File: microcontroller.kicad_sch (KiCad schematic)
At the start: 41 parts, among them U2 W25Q64JVSSIQ, U3 RP2350A, X1 ABM8-272-T3

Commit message: Rev3 fixes
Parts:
- removed R10, R11: 33k, Resistor_SMD:R_0603_1608Metric, symbol Device:R
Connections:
- net CAN_INT: now reaches U3.12 (GPIO8)
- net CAN_RESET: now reaches U3.13 (GPIO9)
- net CAN_STBY: now reaches U3.19 (GPIO15)
- net TX0RTS: now reaches U3.27 (GPIO16)
- net RX0BF: now reaches U3.28 (GPIO17)
- net RX1BF: now reaches U3.29 (GPIO18)
- net SCK: now reaches U3.4 (GPIO2)
- net MOSI: now reaches U3.5 (GPIO3)
- net MISO: now reaches U3.7 (GPIO4)
- net CS: now reaches U3.8 (GPIO5)
- net BUS1.SCL: no longer names the net of U3.35 (GPIO23)
- net BUS1.SDA: no longer names the net of U3.34 (GPIO22)
- no-connect marks 12 -> 6
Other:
- note removed: "I2C0 bus for external comms"
- moved on the sheet: R5, R6, R7, R8, R9

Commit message: Adding in JST XH
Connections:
- net CAN_INT: now also U3.8 (GPIO5); no longer U3.12 (GPIO8)
- net CAN_STBY: no longer U3.19 (GPIO15)
- net CS: now also U3.12 (GPIO8); no longer U3.8 (GPIO5)
- net RX0BF: no longer U3.28 (GPIO17)
- net RX1BF: no longer U3.29 (GPIO18)
- net TX0RTS: no longer U3.27 (GPIO16)
- no-connect marks 6 -> 14

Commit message: Adding JST XH and moving test points
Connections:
- no-connect marks 14 -> 13
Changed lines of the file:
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@@
 		(at 166.37 163.83)
-	)
-	(no_connect
-		(at 59.69 204.47)
 	)
 	(bus_entry

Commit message: Finalizing BOM
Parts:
- R8, R9: value 33k -> 10k; Mfr P/N RC0603FR-0733KL -> RT0603BRD0710KL; Supplier_1 P/N 311-33.0KHRTR-ND -> YAG1236TR-ND; Supplier_1 Unit Price 0.10000 -> 0.11; Supplier_2 P/N C126359 -> C95204; Supplier_2 Unit Price 0.0015 -> 0.0216
- renumbered R12 to R10, R13 to R11, R14 to R12, R15 to R13, R16 to R14, R17 to R15, R18 to R16, R19 to R17, R20 to R18, R21 to R19, U2 to U1, U3 to U2
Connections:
- net +3V3: now also R9.2; no longer R9.1
- net BUS0.SCL: now also R9.1; no longer R9.2

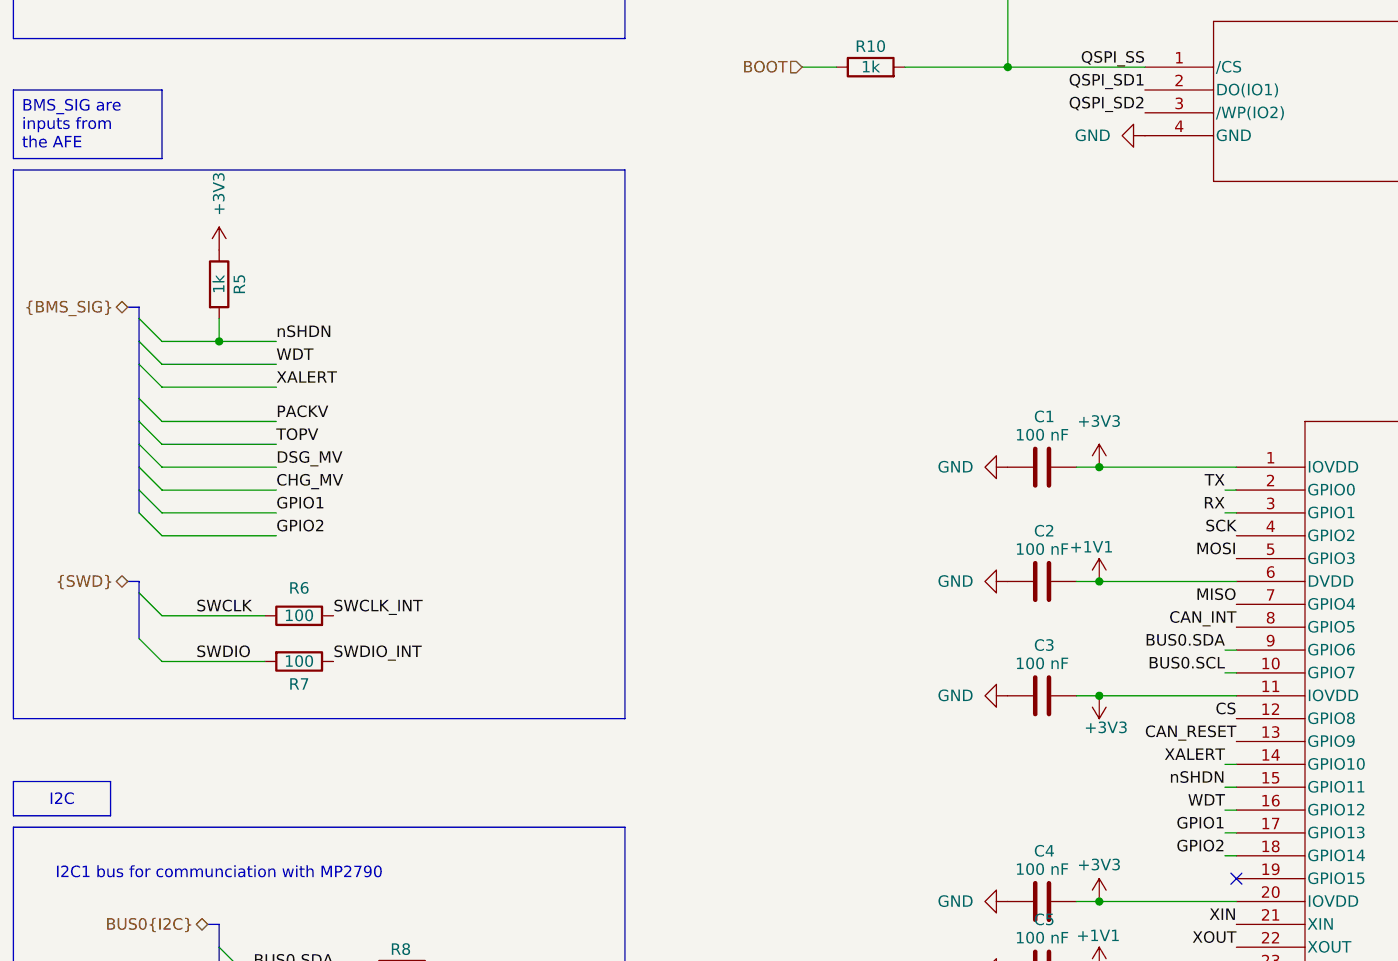
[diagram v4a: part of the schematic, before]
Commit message: rev3: nSHDN wake divider (1M/200k, 10k series to GPIO11), R_REG 100R 2512, 51R balance resistors, NTC ground resistors DNP, SMBJ28CA on TOP, BOM updates
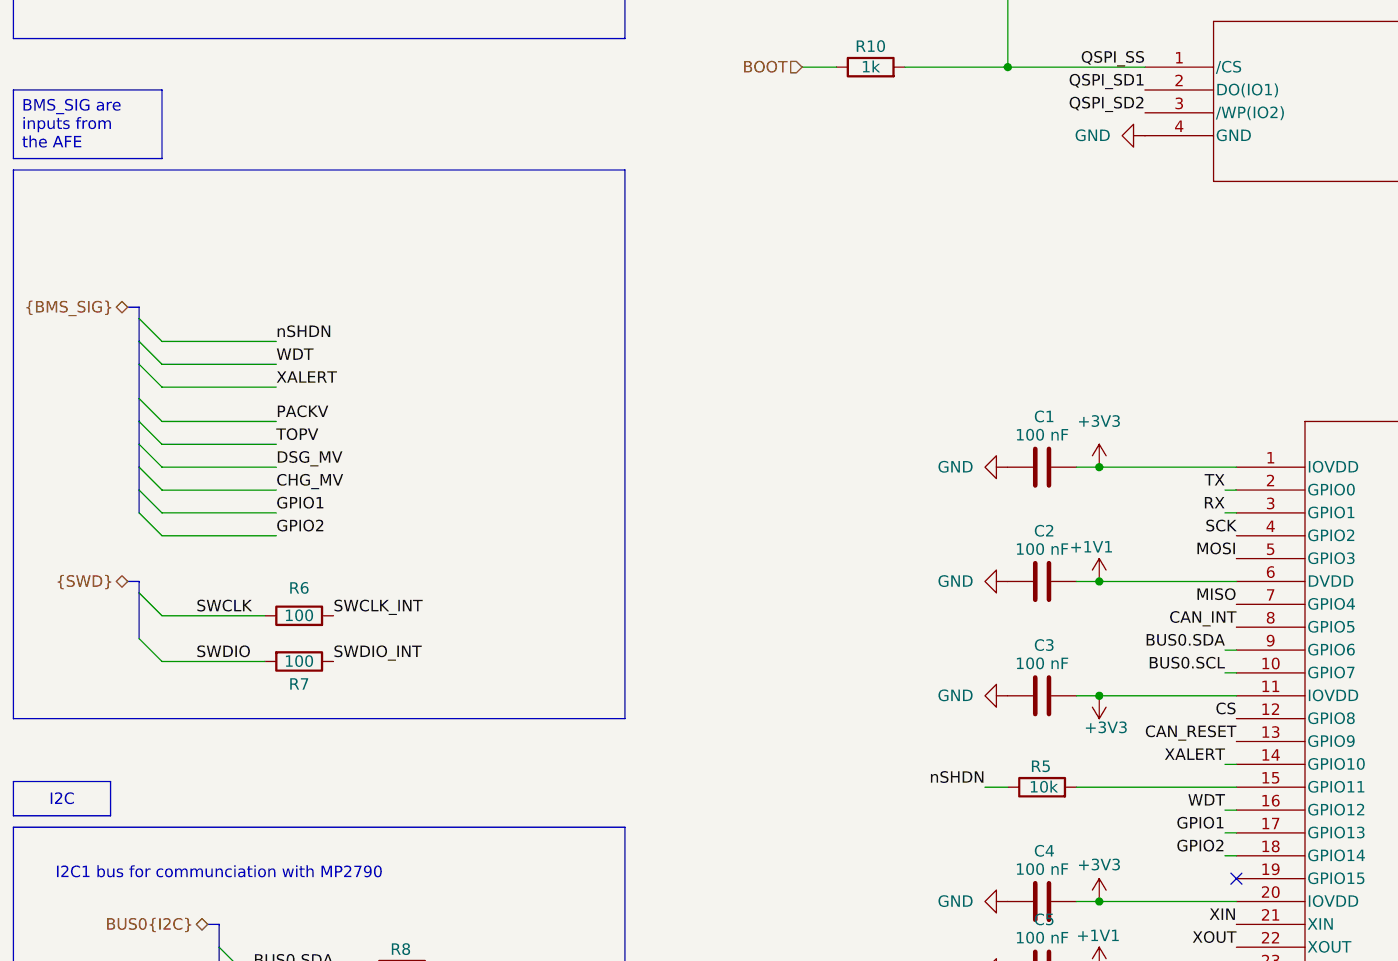
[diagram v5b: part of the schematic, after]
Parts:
- R5: value 1k -> 10k; Mfr P/N AC0603FR-071KL -> RT0603BRD0710KL; Supplier_1 P/N 311-1KLDTR-ND -> YAG1236TR-ND; Supplier_1 Unit Price 0.10000 -> 0.11; Supplier_2 P/N C116692 -> C95204; Supplier_2 Unit Price 0.0025 -> 0.0216
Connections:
- net +3V3: no longer R5.1
- net nSHDN: now also R5.1; no longer R5.2, U2.15 (GPIO11)
- new net: R5.2, U2.15 (GPIO11)
